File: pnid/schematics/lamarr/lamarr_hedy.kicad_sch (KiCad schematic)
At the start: 102 parts

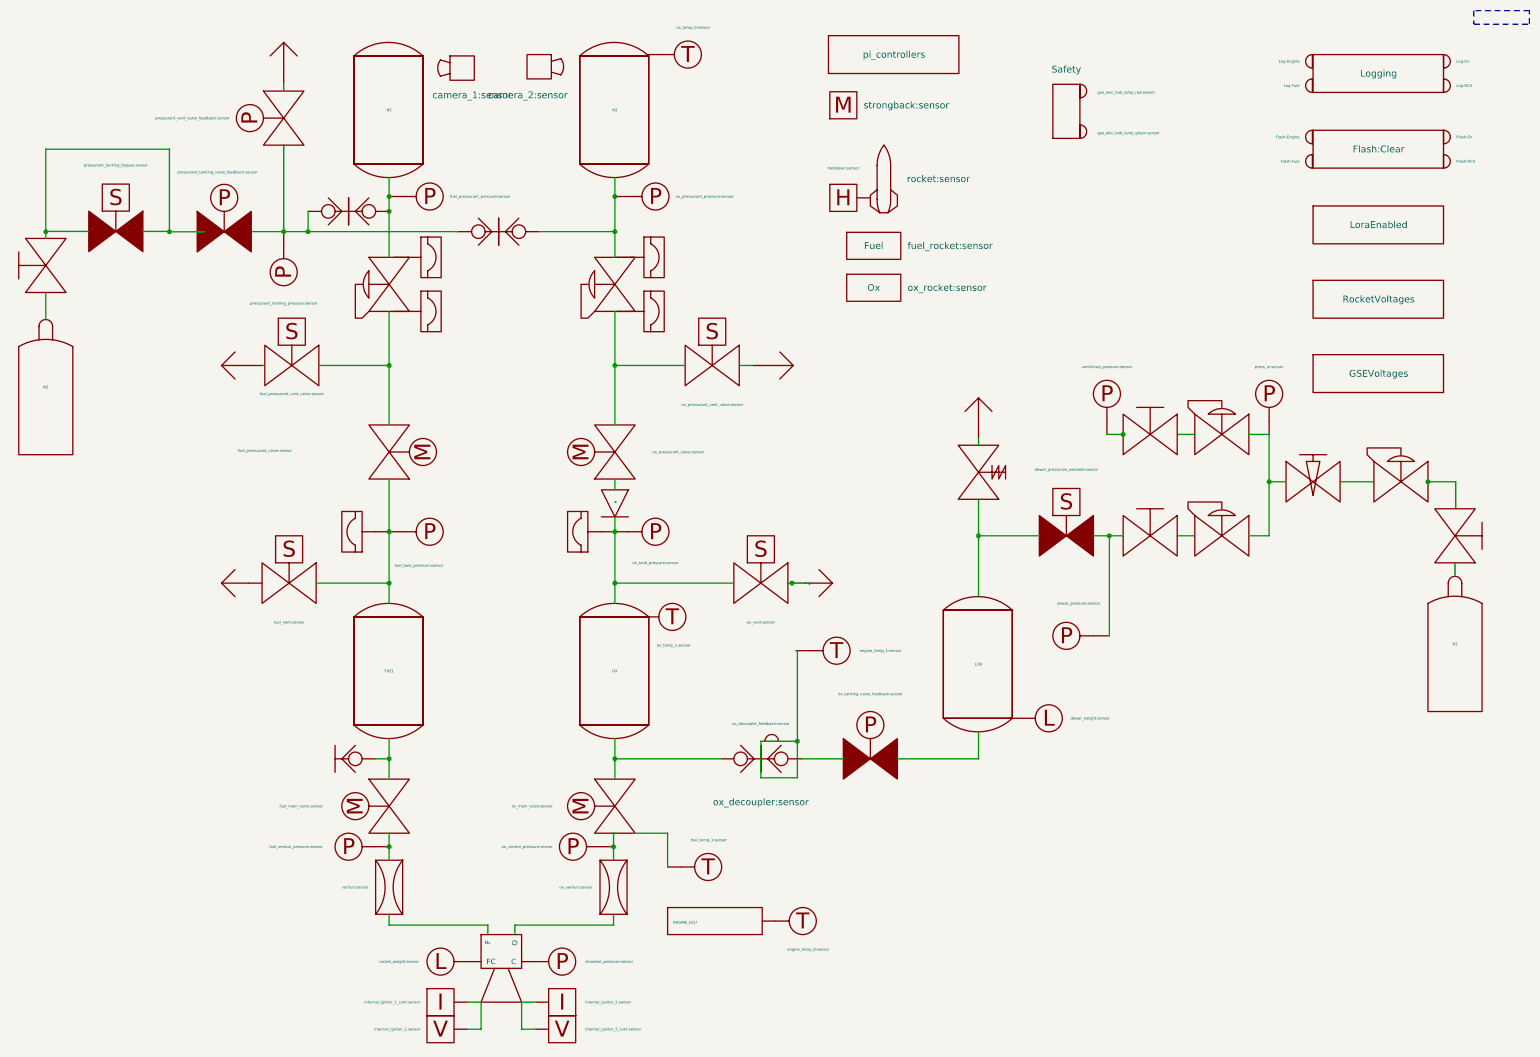
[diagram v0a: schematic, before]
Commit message: optimize pnid label positions
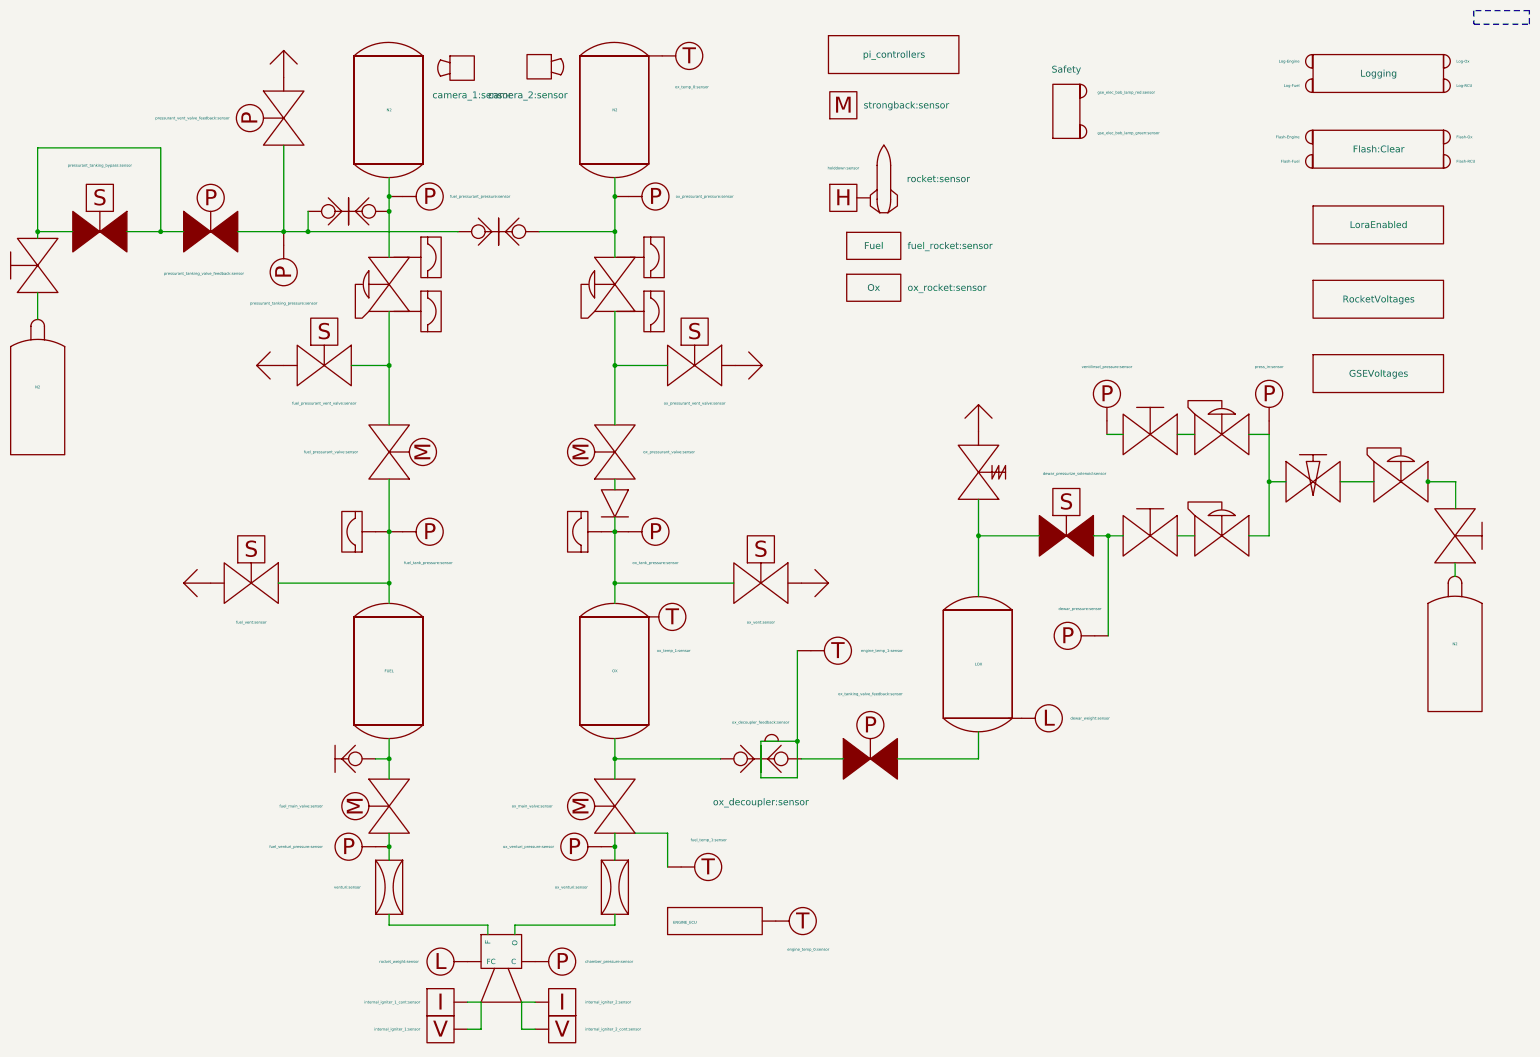
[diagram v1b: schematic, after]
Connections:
- net at engine.~ (C): now also venturi1.~; no longer ox_venturi.~
- net at venturi1.~: now also fuel_main_valve.~, fuel_venturi_pressure.~; no longer engine.~ (C)
- net at dewar_needle_valve?.~: now also C2.~, C3.~; no longer C1.~
- new net: engine.~ (C), ox_venturi.~
- new net: OX.~, ox_main_valve.~, ox_quick_connect.~
- new net: DewarOverPressureValve?.~, LOX.~, dewar_pressurize_solenoid.~
- new net: C1.~, dewar_needle_valve?.~
- new net: ox_pressurant_valve.~, ox_pressurant_vent_valve.~, pressurantPressureRegulator2.~
- new net: FUEL.~, fuel_main_valve.~, ox_quick_connect1.~
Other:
- moved on the sheet: N2

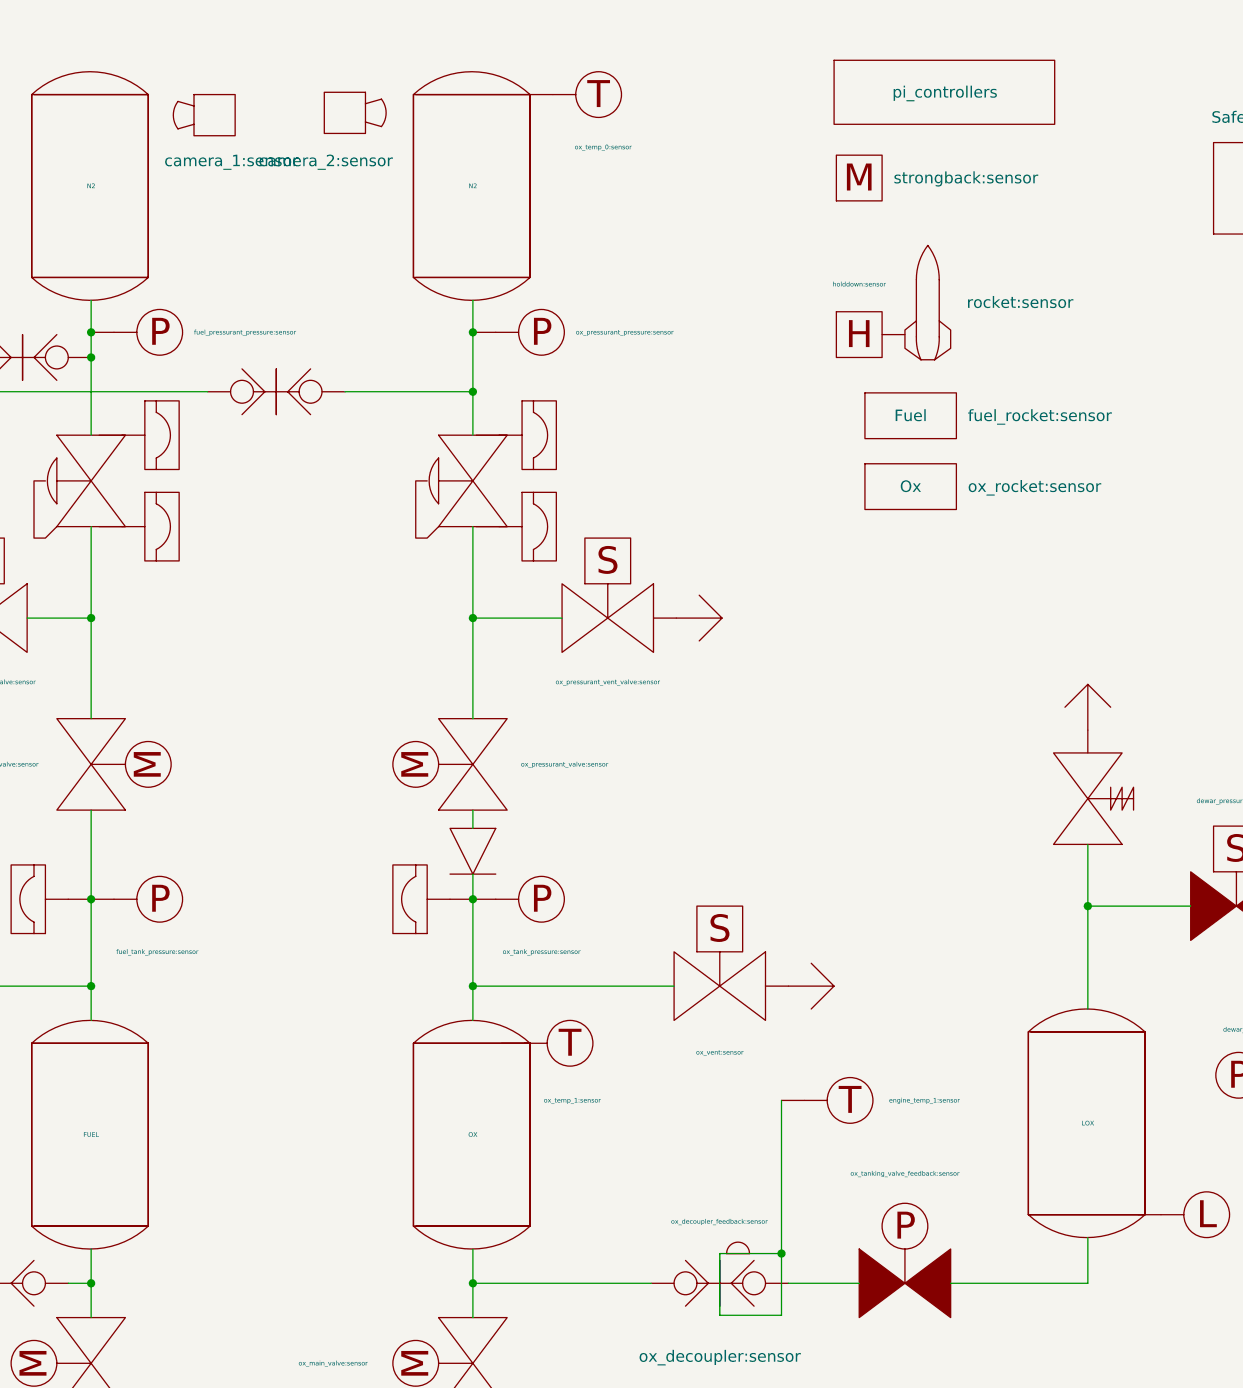
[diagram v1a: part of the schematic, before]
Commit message: update horizontal pnid to reflect vertical changes
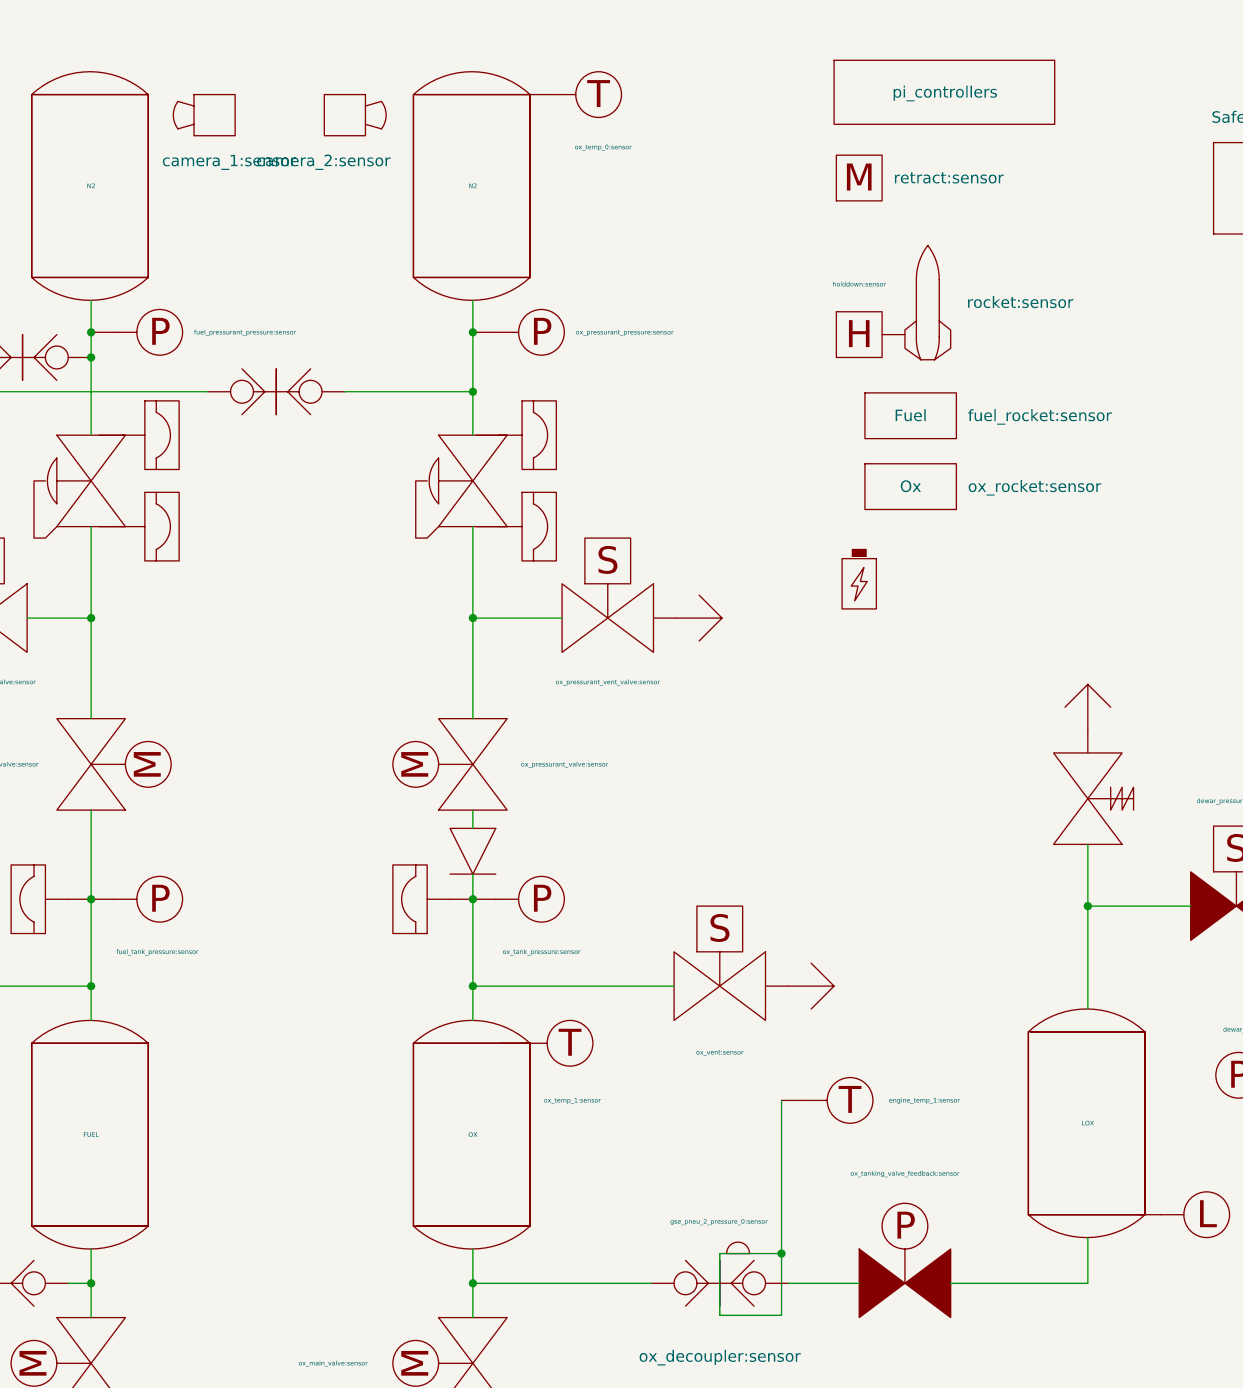
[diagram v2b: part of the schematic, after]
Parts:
- added U2: gse_elec_bob_igniter_2:sensor, symbol PnID-Lib:Battery
- Motor1: value strongback:sensor -> retract:sensor
- ox_decoupler_feedback: value ox_decoupler_feedback:sensor -> gse_pneu_2_pressure_0:sensor
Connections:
- net at engine.~ (C): now also venturi1.~; no longer ox_venturi.~
- net at venturi1.~: now also fuel_main_valve.~, fuel_venturi_pressure.~; no longer engine.~ (C)
- net at dewar_needle_valve?.~: now also C2.~, C3.~; no longer C1.~
- new net: engine.~ (C), ox_venturi.~
- new net: OX.~, ox_main_valve.~, ox_quick_connect.~
- new net: DewarOverPressureValve?.~, LOX.~, dewar_pressurize_solenoid.~
- new net: C1.~, dewar_needle_valve?.~
- new net: ox_pressurant_valve.~, ox_pressurant_vent_valve.~, pressurantPressureRegulator2.~
- new net: FUEL.~, fuel_main_valve.~, ox_quick_connect1.~
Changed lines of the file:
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@@
 	)
 	(symbol
+		(lib_id "PnID-Lib:Battery")
+		(at 163.83 77.47 0)
+		(unit 1)
+		(exclude_from_sim no)
+		(in_bom yes)
+		(on_board yes)
+		(dnp no)
+		(property "Reference" "U2"
+			(at 163.83 70.104 0)
+			(effects
+				(font
+					(size 1.27 1.27)
+				)
+				(hide yes)
+			)
+		)
+		(property "Value" "gse_elec_bob_igniter_2:sensor"
+			(at 163.83 83.82 0)
+			(effects
+				(font
+					(size 1.27 1.27)
+				)
+				(hide yes)
+			)
+		)
+		(property "Footprint" ""
+			(at 164.211 77.47 0)
+			(effects
+				(font
+					(size 1.27 1.27)
+				)
+				(hide yes)
+			)
+		)
+		(property "Datasheet" ""
+			(at 164.211 77.47 0)
+			(effects
+				(font
+					(size 1.27 1.27)
+				)
+				(hide yes)
+			)
+		)
+		(property "Description" ""
+			(at 163.83 77.47 0)
+			(effects
+				(font
+					(size 1.27 1.27)
+				)
+				(hide yes)
+			)
+		)
+		(property "Unit" "V"
+			(at 163.83 77.47 0)
+			(effects
+				(font
+					(size 1.27 1.27)
+				)
+				(hide yes)
+			)
+		)
+		(instances
+			(project "lamarr_hedy"
+				(path "/604fc9f3-63a6-4133-afd1-4a5c2507dc1d"
+					(reference "U2")
+					(unit 1)
+				)
+			)
+		)
+	)
+	(symbol
 		(lib_id "PnID-Lib:PressureRegulator")
 		(at 120.904 66.04 90)
@@
 			)
 		)
-		(property "Value" "strongback:sensor"
+		(property "Value" "retract:sensor"
 			(at 167.64 32.3849 0)
 			(effects
@@
 	(symbol
 		(lib_id "PnID-Lib:Camera")
-		(at 106.68 25.146 0)
+		(at 106.68 25.4 0)
 		(unit 1)
 		(exclude_from_sim no)
@@
 		(dnp no)
 		(property "Reference" "C6"
-			(at 106.68 19.304 0)
+			(at 106.68 19.558 0)
 			(effects
 				(font
@@
 		)
 		(property "Value" "camera_2:sensor"
-			(at 112.014 30.48 0)
+			(at 111.76 30.48 0)
 			(effects
 				(font
@@
 		)
 		(property "Footprint" ""
-			(at 107.442 21.336 0)
+			(at 107.442 21.59 0)
 			(effects
 				(font
@@
 		)
 		(property "Datasheet" ""
-			(at 107.442 21.336 0)
+			(at 107.442 21.59 0)
 			(effects
 				(font
@@
 		)
 		(property "Description" ""
-			(at 106.68 25.146 0)
+			(at 106.68 25.4 0)
 			(effects
 				(font
@@
 			)
 		)
-		(property "Value" "ox_decoupler_feedback:sensor"
+		(property "Value" "gse_pneu_2_pressure_0:sensor"
 			(at 153.67 148.336 0)
 			(effects
@@
 		)
 		(property "Value" "camera_1:sensor"
-			(at 86.614 30.48 0)
+			(at 86.36 30.48 0)
 			(effects
 				(font
